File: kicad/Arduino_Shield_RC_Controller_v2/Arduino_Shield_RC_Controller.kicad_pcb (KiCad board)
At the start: 2 copper layers, 135 x 100 mm, 17 parts, among them J1 CONN_04X2, SW1 PTS810SJG250SMTRLFS, SW2 PTS810SJG250SMTRLFS, SW3 PTS810SJG250SMTRLFS, SW4 PTS810SJG250SMTRLFS, SW5 PTS810SJG250SMTRLFS, SW6 SW_Omron_B3FS

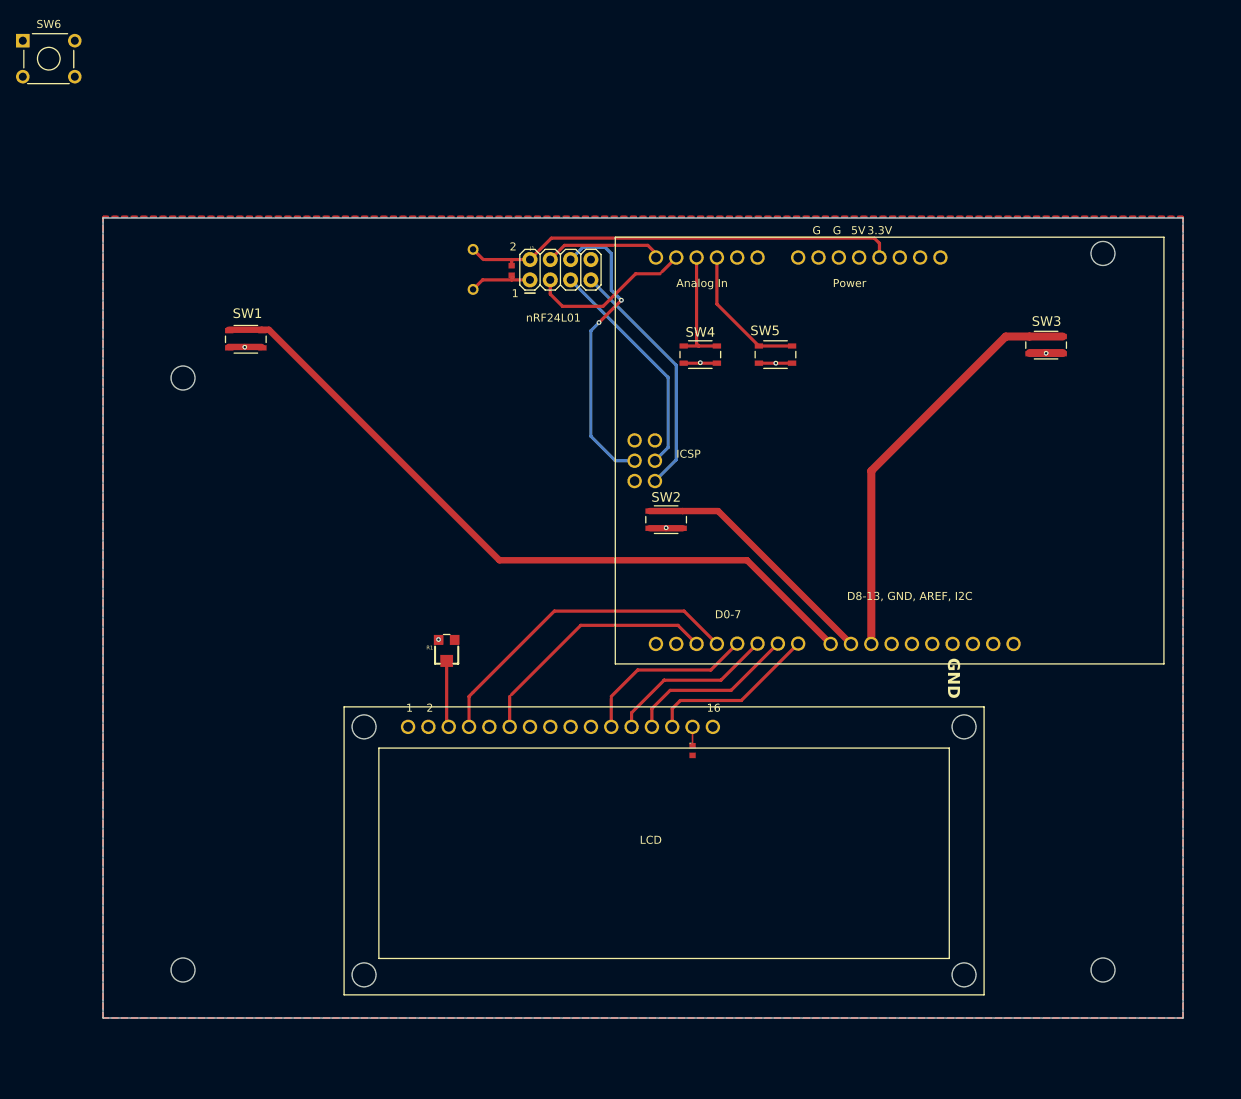
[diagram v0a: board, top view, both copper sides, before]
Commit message: starting the Hobby RC and Motor Control shield
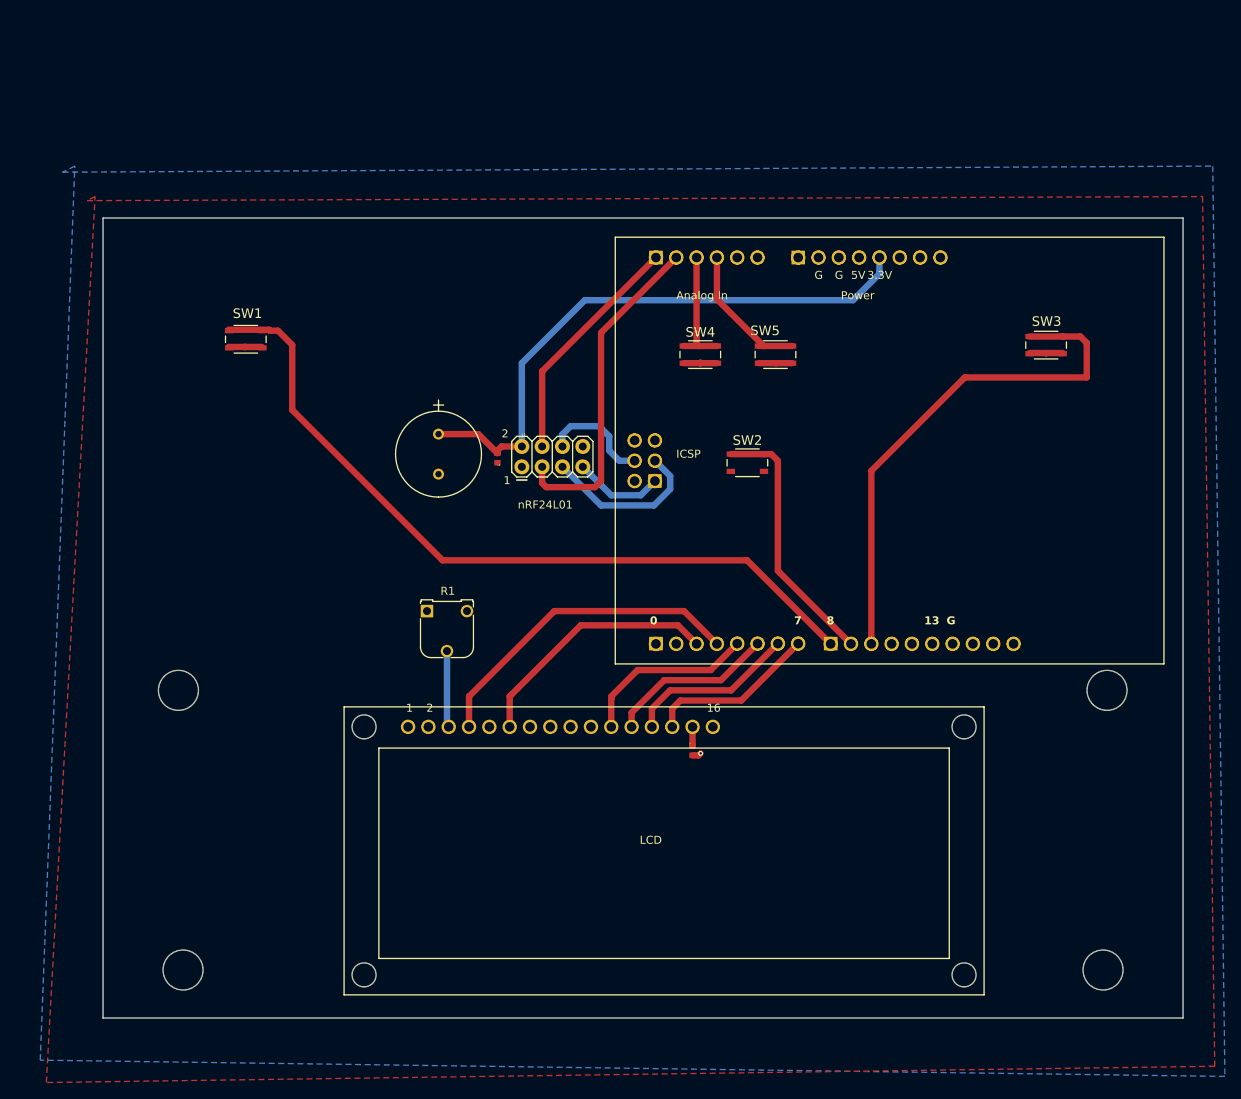
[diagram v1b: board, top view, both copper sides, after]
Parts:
- removed SW6: SW_Omron_B3FS, Button_Switch_THT:SW_TH_Tactile_Omron_B3F-10xx
- added J2: Conn_01x08_Pin, Connector_PinHeader_2.54mm:PinHeader_1x08_P2.54mm_Vertical, B.Cu at (150.1, 108.2)
- added J3: Conn_01x10_Pin, Connector_PinHeader_2.54mm:PinHeader_1x10_P2.54mm_Vertical, B.Cu at (172.0, 108.2)
- added J4: Conn_01x06_Pin, Connector_PinHeader_2.54mm:PinHeader_1x06_P2.54mm_Vertical, B.Cu at (150.1, 59.9)
- added J5: Conn_01x08_Pin, Connector_PinHeader_2.54mm:PinHeader_1x08_P2.54mm_Vertical, B.Cu at (167.9, 59.9)
- added J6: Conn_02x03_Odd_Even, Connector_PinSocket_2.54mm:PinSocket_2x03_P2.54mm_Vertical, B.Cu at (150.0, 87.9)
- C2: moved to F.Cu
- R1: footprint Arduino_Shield_RC_Controller:RTRIM3103 -> Potentiometer_THT:Potentiometer_Runtron_RM-065_Vertical
- moved @HOLE2 54.6 mm to (206.5, 114.0)
- moved @HOLE3 39.0 mm to (90.4, 114.0)
- moved C1 23.5 mm to (130.3, 85.0)
- moved C2 23.5 mm to (122.9, 82.0)
- moved J1 23.4 mm to (137.2, 84.8)
- moved SW2 12.4 mm to (161.5, 85.6)
- moved R1 5.42 mm to (121.5, 104.1), turned to 0 degrees
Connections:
- AR1 pad P20: unconnected-(AR1-VDD5-PadP20) -> Net-(AR1-VDD5)
- AR1 pad P23: unconnected-(AR1-RESET2-PadP23) -> Net-(AR1-RESET2)
- AR1 pad P24: unconnected-(AR1-GND3-PadP24) -> Net-(AR1-GND3)
- AR1 pad P29: unconnected-(AR1-A1-PadP29) -> Net-(AR1-A1)
- AR1 pad P30: unconnected-(AR1-A0-PadP30) -> Net-(AR1-A0)
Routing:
- net /MOSI: track 37.7 -> 13.8 mm, vias 2 -> 0
- net Net-(AR1-A4): track 20.7 -> 41.8 mm
- net /MISO: track 30.7 -> 11.2 mm
- net +3.3V: track 55.2 -> 73.7 mm
- net Net-(AR1-A5): track 14.9 -> 29.5 mm
- net Net-(AR1-10): track 52.5 -> 65.2 mm
- net GND: track 29.1 -> 17.1 mm, vias 6 -> 0
- net Net-(AR1-SCK/PB5): track 28.3 -> 20.6 mm
- net Net-(AR1-8): track 91.5 -> 96.3 mm
- net +5V: track 0.00 -> 1.37 mm, vias 0 -> 1
- net /V0: track 8.35 -> 9.56 mm
- net Net-(AR1-9): track 32.1 -> 32.9 mm
- added copper zone on F.Cu, net GND
- removed copper zone on F.Cu, net +5V
- removed copper zone on B.Cu, net GND
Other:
- board text added: "0"
- board text added: "13"
- board text added: "7"
- board text added: "8"
- board text removed: "D0-7"
- board text removed: "D8-13, GND, AREF, I2C"
- board text removed: "GND"
